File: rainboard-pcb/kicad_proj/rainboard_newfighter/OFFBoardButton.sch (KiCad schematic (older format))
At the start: 5 parts

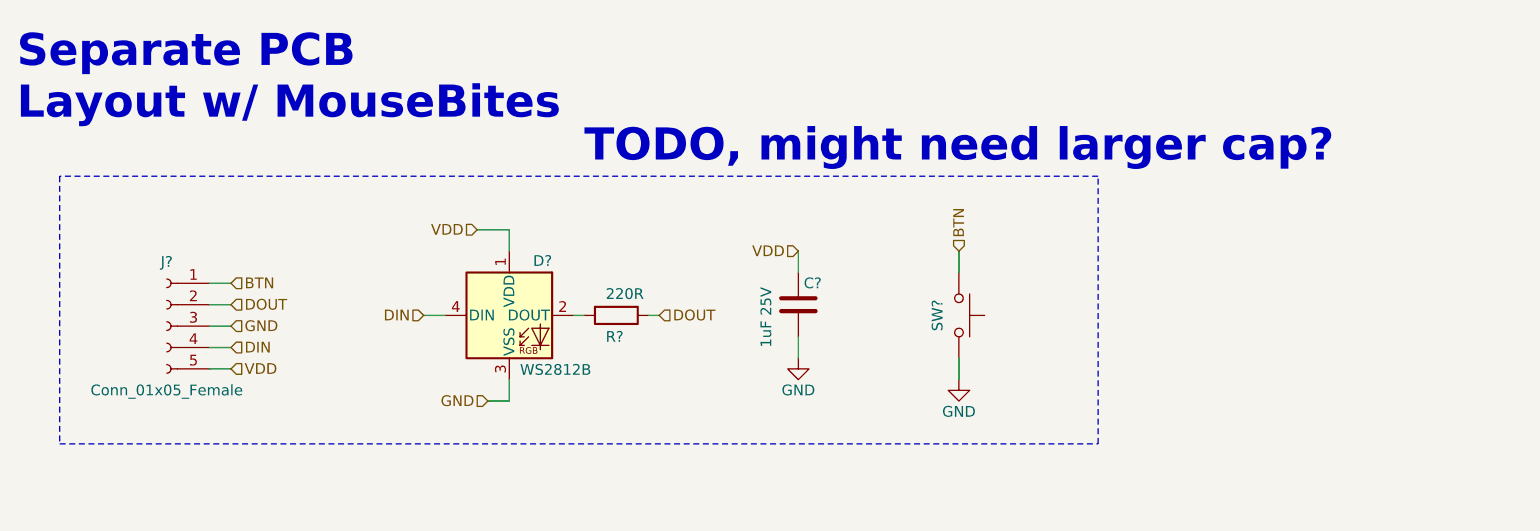
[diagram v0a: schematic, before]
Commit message: Schematic nearly finalized; PCB / footprint started
-Schematic is nearly finished. Needs some footprint associations and verifications.
-A few open questions remain.
-some lib updates to go w/ sch improvements
-
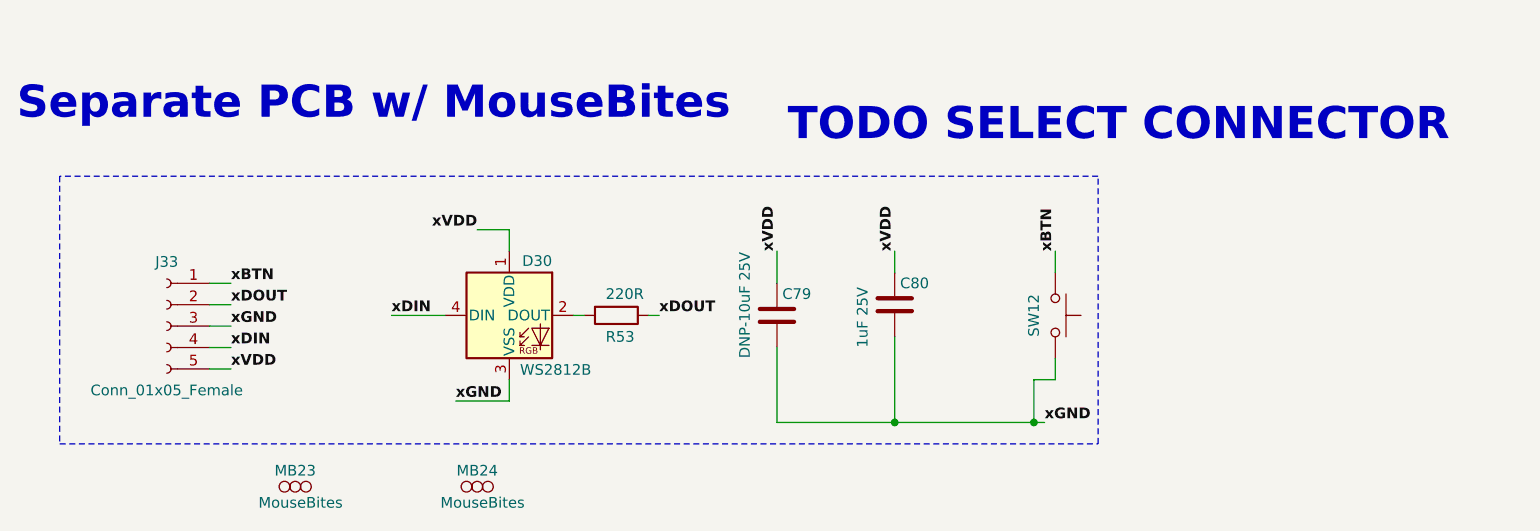
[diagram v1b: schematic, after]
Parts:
- added C69: DNP-10uF 25V, Capacitor_SMD:C_1206_3216Metric, symbol lib_symbol:C
- added MB13, MB14: MouseBites, symbol lib_symbol:MouseBites
- SW1: renamed from SW?; PN (none) -> SANWA-OBSC-CW/W
- gave numbers to parts that had none: 4
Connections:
- net BTN renamed xBTN
- net DIN renamed xDIN
- net DOUT renamed xDOUT
- net GND renamed xGND
- net xGND: now also C69.2
- net VDD renamed xVDD
- net xVDD: now also C69.1
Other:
- note added: "Separate PCB w/ MouseBites"
- note added: "TODO SELECT CONNECTOR\n"
- note removed: "Separate PCB\nLayout w/ MouseBites"
- note removed: "TODO, might need larger cap?"
- moved on the sheet: C80, SW12
